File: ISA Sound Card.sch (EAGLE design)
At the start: 60 parts, among them IC1 74LS07D, IC2 74AHC1G07DBV, U1 PCM1808, U10 SN74LVC16T245DGGR, U11 SN74LVC16T245DGGR, U12 SN74LVC16T245DGGR, U3 MIC5365-3.3YD5-TR, U4 PCM5102, U5 SN74LVC16T245DGGR, U7 MIC5365-3.3YD5-TR, U8 SN74LVC16T245DGGR, U9 SN74LVC16T245DGGR, X2 LINE_OUT, X3 LINE_IN

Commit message: First routing done, DRC passed. MIDI and Waveblaster are todo
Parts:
- removed F1, F2: 500mA, adafruit:PTCFUSE-1206
- added C10, C11, C12, C13, C14, C3, C4, C5, C6, C7, C8, C9: 100nF, rcl:C-EUC0603
- added F3, F5, F6: 500mA, adafruit:PTCFUSE-1206
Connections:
- removed net -5V: ISAB.-5VDC
- new net MIDI_RXD: U$512.F
- new net MIDI_TXD: U$515.F
- new net N$13: F3.2, ISAB.+5VDC@1
- new net N$14: F5.2, ISAB.-12VDC
- new net N$27: F6.2, ISAB.+12VDC
- net +12V: now also F5.1; no longer ISAB.-12VDC
- net +3V3: now also C10.1, C11.1, C12.1, C13.1, C14.1, C9.1, U$1G$1.+3V3@3, U$1G$1.+3V3@4, U$1G$2.+3V3@3, U$1G$2.+3V3@4
- net +5V: now also C3.1, C4.1, C5.1, C6.1, C7.1, C8.1, F3.1, JP1.10, JP1.14, JP1.6, U$51.F, U$58.F, U$59.F; no longer F1.2, F2.2, ISAB.+5VDC@1
- net -12V: now also F6.1; no longer ISAB.+12VDC
- net GND: now also C10.2, C11.2, C12.2, C13.2, C14.2, C3.2, C4.2, C5.2, C6.2, C7.2, C8.2, C9.2; no longer U$512.F
- net N$5: now also U$1G$3.FPGA_DCLK; no longer F1.1, JP1.10, JP1.14, JP1.6
- net N$6: now also U$1G$3.FPGA_ADS0; no longer F2.1, U$51.F, U$515.F, U$58.F, U$59.F
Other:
- note added: "TODO - MIDI voltage translation and FPGA hookup"
- moved on the sheet: ISAA, ISAB, ISAC, ISAD, R1, R2, R3, U10, U11, U12, U5, U8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

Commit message: Had to change IRQ/DRQ buffers for muxes. Not routed yet
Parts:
- removed F5, F6: 500mA, adafruit:PTCFUSE-1206
- removed JP1: (no value), pinhead:PINHD-2X13
- removed U5, U9: SN74LVC16T245DGGR, SN74LVC16T245DGGR:SN74LVC16T245DGGR
- added C15, C16, C17, C18: 100nF, rcl:C-EUC0805
- added C19, C20, C21, C22: 100nF, rcl:C-EUC0603
- added IC10, IC11, IC8, IC9: 4051D, 40xx:4051D
- added IC3: 74AC14D, 74xx-eu:74AC14D
- added IC4: 74LVC1G125DBV, 74xx-little-de:74LVC1G125DBV
- added R10, R7, R8, R9: 4K7, rcl:R-EU_R0603
- added RN2: 10K, resistor-dil:4R-N0603-ARC
- added RN3: 2K2, resistor-dil:4R-N0603-ARC
- added U$2: MCP3004, adafruit:MCP3004
- RN1: value (none) -> 2K2
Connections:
- net N$5 renamed FPGA_DCLK
- net N$6 renamed FPGA_ADS0
- removed net +12V: F5.1, JP1.18
- removed net -12V: F6.1, JP1.22
- removed net FPGA_DRQ0: U$1G$2.BANK4A_U17, U5.1B8
- removed net FPGA_DRQ1: U$1G$1.BANK7A_H11, U9.2B1
- removed net FPGA_DRQ2: U$1G$2.BANK3B_U12, U9.1B6
- removed net FPGA_DRQ3: U$1G$2.BANK3B_V9, U9.1B8
- removed net FPGA_DRQ5: U$1G$1.BANK7A_C18, U5.2B1
- removed net FPGA_DRQ6: U$1G$2.BANK4A_AB17, U5.2B2
- removed net FPGA_DRQ7: U$1G$1.BANK7A_C19, U5.2B3
- removed net FPGA_IRQ10: U$1G$1.BANK7A_B18, U5.1B3
- removed net FPGA_IRQ11: U$1G$2.BANK5A_R16, U5.1B4
- removed net FPGA_IRQ12: U$1G$1.BANK7A_A17, U5.1B5
- removed net FPGA_IRQ14: U$1G$1.BANK7A_A18, U5.1B7
- removed net FPGA_IRQ15: U$1G$2.BANK4A_U16, U5.1B6
- removed net FPGA_IRQ3: U$1G$2.BANK3B_AB11, U9.2B6
- removed net FPGA_IRQ4: U$1G$1.BANK7A_D12, U9.2B5
- removed net FPGA_IRQ5: U$1G$2.BANK3B_AB10, U9.2B4
- removed net FPGA_IRQ6: U$1G$1.BANK7A_E12, U9.2B3
- removed net FPGA_IRQ7: U$1G$2.BANK3B_V10, U9.2B2
- removed net FPGA_IRQ9: U$1G$1.BANK8A_A10, U9.1B5
- removed net GAME_B1_N: U$52.F
- removed net GAME_B2_N: U$57.F
- removed net GAME_B3_N: U$510.F
- removed net GAME_B4_N: U$514.F
- removed net GAME_X1: U$53.F
- removed net GAME_X2: U$511.F
- removed net GAME_Y: U$513.F
- removed net GAME_Y1: U$56.F
- removed net N$10: U$1G$1.BANK8A_B6
- removed net N$12: U$1G$1.BANK8A_J7
- removed net N$16: U$1G$2.BANK3A_N6
- removed net N$17: U$1G$2.BANK3A_R5
- removed net N$18: U$1G$2.BANK3A_M6
- removed net N$19: U$1G$2.BANK3A_P6
- removed net N$20: U$1G$2.BANK3A_R6
- removed net N$26: U$1G$2.BANK3B_AA8
- removed net N$3: U$1G$1.BANK8A_A5
- removed net N$4: U$1G$1.BANK8A_C6
- removed net N$7: U$1G$2.BANK4A_AB18
- removed net WAVL: JP1.20
- removed net WAVR: JP1.24
- removed net WAV_MIDI: JP1.4
- removed net WAV_RST_N: JP1.26
- new net DRQ_HI_SEL_A0: IC11A.A, U$1G$1.BANK7A_C18
- new net DRQ_HI_SEL_A1: IC11A.B, U$1G$1.BANK7A_A18
- new net DRQ_HI_SEL_A2: IC11A.C, U$1G$1.BANK7A_A17
- new net DRQ_HI_TRIG_N: IC11A.INH, R10.1, U$1G$1.BANK7A_C19
- new net DRQ_LO_SEL_A0: IC10A.A, U$1G$2.BANK4A_AB17
- new net DRQ_LO_SEL_A1: IC10A.B, U$1G$2.BANK4A_U17
- new net DRQ_LO_SEL_A2: IC10A.C, U$1G$2.BANK4A_U16
- new net DRQ_LO_TRIG_N: IC10A.INH, R9.1, U$1G$2.BANK4A_AB18
- new net FPGA_JOY_B1: IC3A.O, U$1G$2.BANK3A_M6
- new net FPGA_JOY_B2: IC3B.O, U$1G$2.BANK3A_N6
- new net FPGA_JOY_B3: IC3C.O, U$1G$2.BANK3A_P6
- new net FPGA_JOY_B4: IC3D.O, U$1G$2.BANK3A_R5
- new net FPGA_MIDI_RXD: IC3E.O, U$1G$2.BANK3A_R6
- new net FPGA_MIDI_TXD: IC4A.I, U$1G$2.BANK3B_AA8
- new net IRQ_HI_SEL_A0: IC9A.A, U$1G$1.BANK7A_E12
- new net IRQ_HI_SEL_A1: IC9A.B, U$1G$1.BANK7A_H11
- new net IRQ_HI_SEL_A2: IC9A.C, U$1G$1.BANK8A_A10
- new net IRQ_HI_TRIG_N: IC9A.INH, R8.1, U$1G$1.BANK7A_D12
- new net IRQ_LO_SEL_A0: IC8A.A, U$1G$2.BANK3B_AB11
- new net IRQ_LO_SEL_A1: IC8A.B, U$1G$2.BANK3B_V9
- new net IRQ_LO_SEL_A2: IC8A.C, U$1G$2.BANK3B_V10
- new net IRQ_LO_TRIG_N: IC8A.INH, R7.1, U$1G$2.BANK3B_AB10
- new net JOY_B1_N: IC3A.I, U$52.F
- new net JOY_B2_N: IC3B.I, U$57.F
- new net JOY_B3_N: IC3C.I, U$510.F
- new net JOY_B4_N: IC3D.I, U$514.F
- new net JOY_CLK: U$1G$1.BANK8A_C6, U$2.CLK
- new net JOY_CS_N: U$1G$1.BANK8A_J7, U$2./CS
- new net JOY_DIN: U$1G$1.BANK8A_A8, U$2.DIN
- new net JOY_DOUT: U$1G$1.BANK8A_B6, U$2.DOUT
- new net JOY_X1: RN2A.1, U$53.F
- new net JOY_X2: RN2B.1, U$511.F
- new net JOY_Y1: RN2D.1, U$56.F
- new net JOY_Y2: RN2C.1, U$513.F
- new net N$15: RN2D.2, RN3A.2, U$2.CH3
- new net N$28: RN2C.2, RN3B.2, U$2.CH2
- new net N$31: RN2B.2, RN3C.2, U$2.CH1
- new net N$32: RN2A.2, RN3D.2, U$2.CH0
- new net N$34: IC3F.O
- new net N$41: IC3F.I
- net +3V3: now also C15.1, C16.1, C17.1, IC3P.VCC, R10.2, R7.2, R8.2, R9.2, U$2.VDD, U$2.VREF; no longer U5.VCCB_18, U5.VCCB_7, U9.VCCB_18, U9.VCCB_7
- net +5V: now also C18.1, C19.1, C20.1, C21.1, C22.1, IC10A.X, IC10P.VCC, IC11A.X, IC11P.VCC, IC4P.VCC, IC8A.X, IC8P.VCC, IC9A.X, IC9P.VCC; no longer JP1.10, JP1.14, JP1.6, U5.VCCA_31, U5.VCCA_42, U9.VCCA_31, U9.VCCA_42
- net DRQ0: now also IC10A.X0, IC11A.X0; no longer U5.1A8
- net DRQ1: now also IC10A.X1, IC11A.X1; no longer U9.2A1
- net DRQ2: now also IC10A.X2, IC11A.X2; no longer U9.1A6
- net DRQ3: now also IC10A.X3, IC11A.X3; no longer U9.1A8
- net DRQ5: now also IC10A.X5, IC11A.X5; no longer U5.2A1
- net DRQ6: now also IC10A.X6, IC11A.X6; no longer U5.2A2
- net DRQ7: now also IC10A.X7, IC11A.X7; no longer U5.2A3
- net FPGA_SD70_DIR: now also U$1G$1.BANK8A_A5; no longer U$1G$1.BANK8A_A8
- net GND: now also C15.2, C16.2, C17.2, C18.2, C19.2, C20.2, C21.2, C22.2, IC10P.GND, IC10P.VEE, IC11P.GND, IC11P.VEE, IC3P.GND, IC4A.OE, IC4P.GND, IC8P.GND, IC8P.VEE, IC9P.GND, IC9P.VEE, RN3A.1, RN3B.1, RN3C.1, RN3D.1, U$2.AGND, U$2.DGND; no longer JP1.1, JP1.11, JP1.15, JP1.17, JP1.19, JP1.21, JP1.23, JP1.25, JP1.3, JP1.5, JP1.7, JP1.9, U5.1!OE, U5.1DIR, U5.2!OE, U5.2DIR, U5.GND_10, U5.GND_15, U5.GND_21, U5.GND_28, U5.GND_34, U5.GND_39, U5.GND_4, U5.GND_45, U9.1!OE, U9.1DIR, U9.2!OE, U9.2DIR, U9.GND_10, U9.GND_15, U9.GND_21, U9.GND_28, U9.GND_34, U9.GND_39, U9.GND_4, U9.GND_45
- net IRQ10: now also IC8A.X3, IC9A.X3; no longer U5.1A3
- net IRQ11: now also IC8A.X4, IC9A.X4; no longer U5.1A4
- net IRQ12: now also IC8A.X5, IC9A.X5; no longer U5.1A5
- net IRQ14: now also IC8A.X6, IC9A.X6; no longer U5.1A7
- net IRQ15: now also IC8A.X7, IC9A.X7; no longer U5.1A6
- net IRQ3: no longer U9.2A6
- net IRQ4: no longer U9.2A5
- net IRQ5: now also IC8A.X0, IC9A.X0; no longer U9.2A4
- net IRQ6: now also IC8A.X1, IC9A.X1; no longer U9.2A3
- net IRQ7: now also IC8A.X2, IC9A.X2; no longer U9.2A2
- net IRQ9: no longer U9.1A5
- net MIDI_RXD: now also IC3E.I
- net MIDI_TXD: now also IC4A.O
- net N$14: no longer F5.2
- net N$27: no longer F6.2
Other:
- note removed: "<- OUTPUTS"
- note removed: "TODO - MIDI voltage translation and FPGA hookup"
- note removed: "WaveBlaster Header"

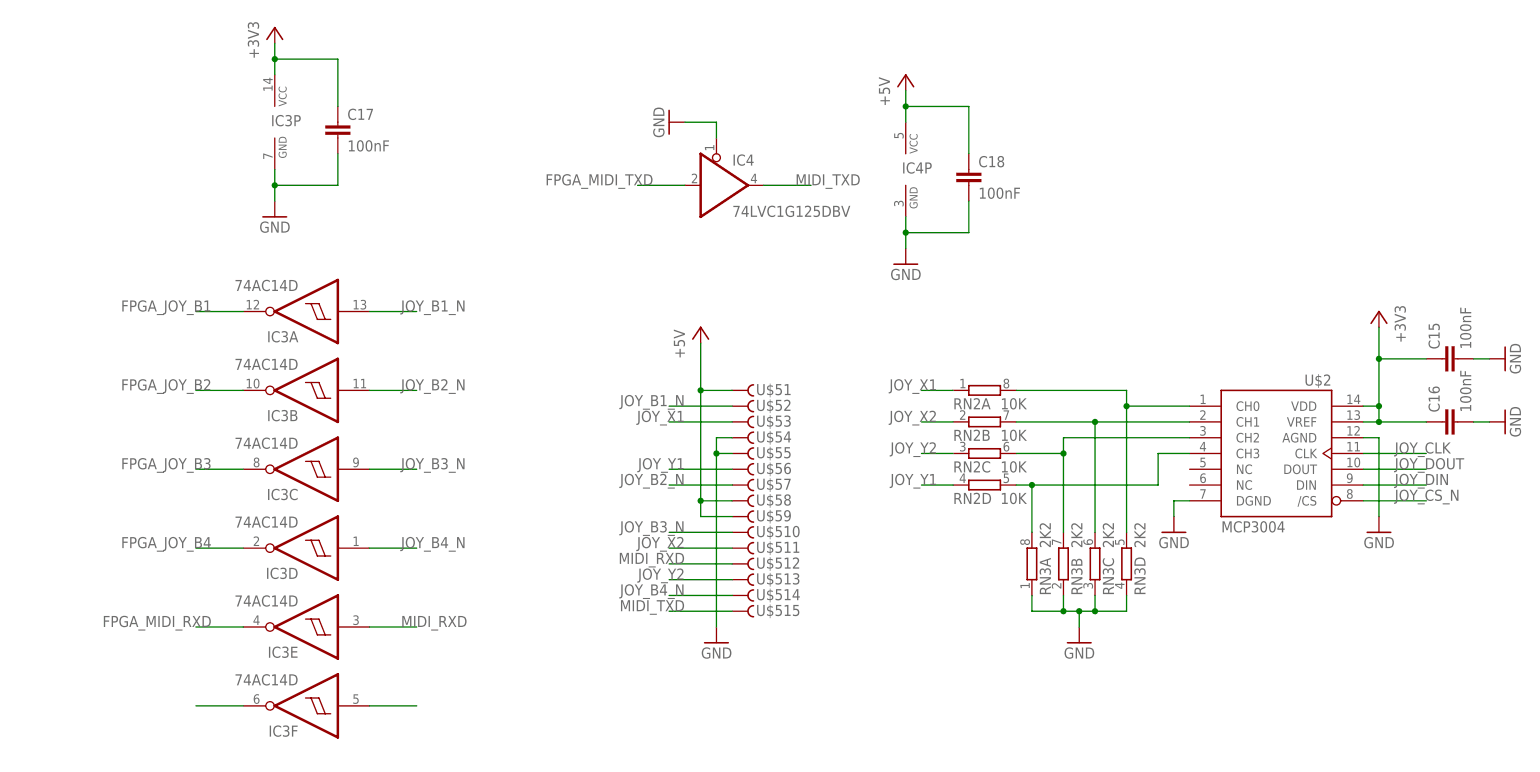
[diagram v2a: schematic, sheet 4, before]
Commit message: Routing done. Fixed two missing signals. Five proto PCBs being made by JLC
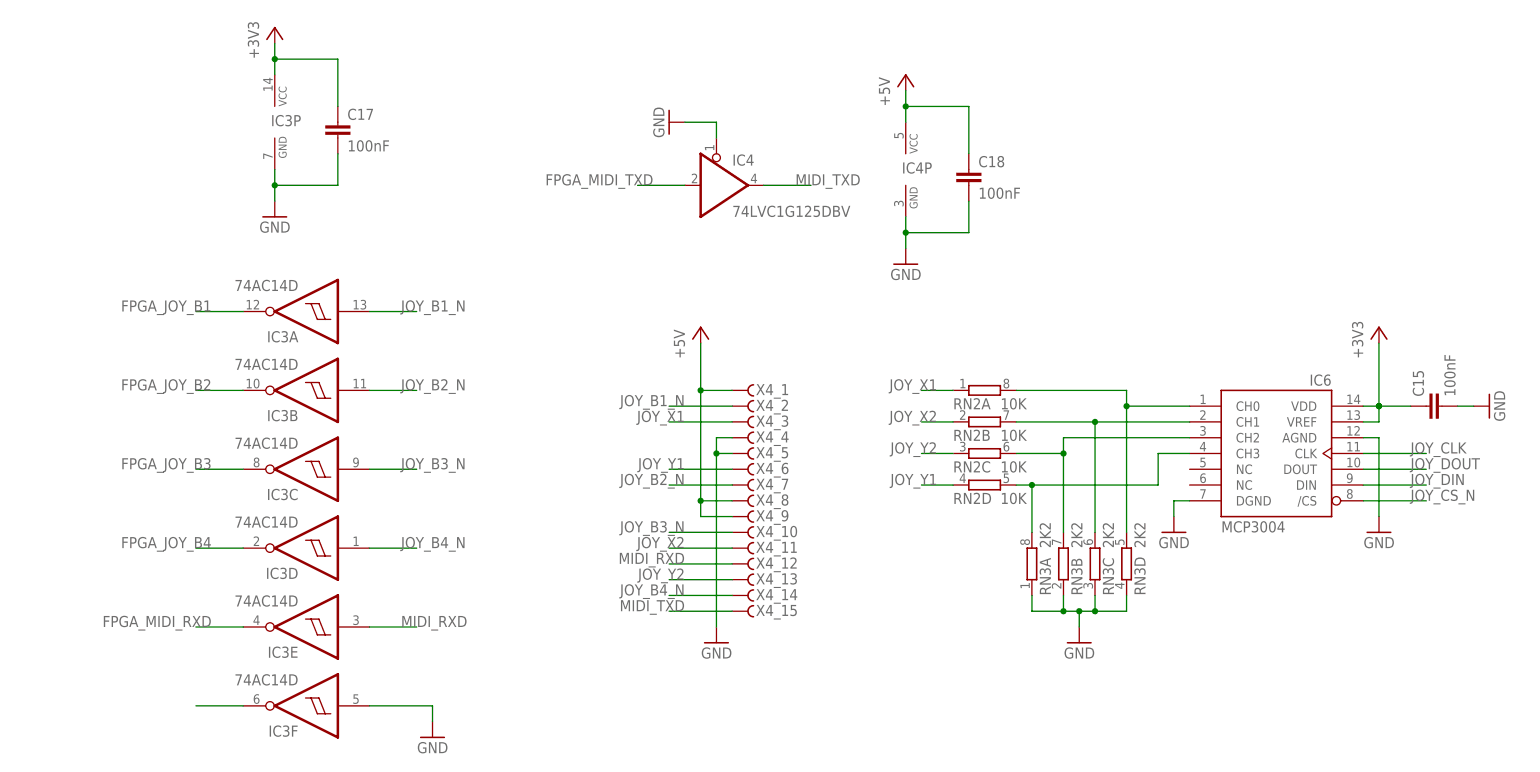
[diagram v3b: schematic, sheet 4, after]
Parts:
- removed C16: 100nF, rcl:C-EUC0805
- added R11: 4K7, rcl:R-EU_R0603
- renumbered U$2 to IC6, U$5 to X4_
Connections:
- removed net +5VDC: ISAD.+5VDC
- removed net FPGA_MEMW_R: U11.1B2
- removed net N$11: U$1G$1.BANK7A_A14
- removed net N$41: IC3F.I
- new net FPGA_MEMW_N: U$1G$1.BANK7A_A15, U11.1B2
- new net FPGA_SA159_DIR: R11.2, U$1G$2.BANK3B_U12, U8.1DIR, U8.2DIR
- net +3V3: now also R11.1; no longer C16.1, U8.1DIR, U8.2DIR
- net +5V: now also ISAD.+5VDC
- net FPGA_BALE: now also U$1G$1.BANK7A_C16; no longer U$1G$1.BANK7A_C15
- net FPGA_DACK0_N: now also U$1G$1.BANK7A_B16; no longer U$1G$1.BANK7A_C16
- net FPGA_DACK2_N: now also U$1G$1.BANK7A_C15; no longer U$1G$1.BANK7A_B15
- net FPGA_DACK3_N: now also U$1G$1.BANK7A_E15; no longer U$1G$1.BANK7A_F15
- net FPGA_DACK6_N: now also U$1G$1.BANK7A_B18; no longer U$1G$1.BANK7A_B16
- net FPGA_IOW_N: now also U$1G$1.BANK7A_F15; no longer U$1G$1.BANK7A_A15
- net FPGA_MEMR_N: now also U$1G$1.BANK7A_A14
- net FPGA_SD159_DIR: now also U$1G$1.BANK7A_B15; no longer U$1G$1.BANK7A_E15
- net GND: now also IC3F.I; no longer C16.2
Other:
- note added: "INPUTS -> (Added DIR control anyway)"
- moved on the sheet: C15

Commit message: Updated Eagle symbols for the QMTech CycIV version
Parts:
- removed U$1: QMTECH_5CEFA5F23_SMD, qmtech:QMTECH_5CEFA5F23_SMD
- added CYC_IV_: QMTECH_EP4CE15, qmtech:QMTECH_EP4CE15
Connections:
- net +3V3: now also CYC_IV_G$1.+3V3@3, CYC_IV_G$1.+3V3@4, CYC_IV_G$2.+3V3@3, CYC_IV_G$2.+3V3@4; no longer U$1G$1.+3V3@3, U$1G$1.+3V3@4, U$1G$2.+3V3@3, U$1G$2.+3V3@4
- net +5V: now also CYC_IV_G$1.VIN@63, CYC_IV_G$1.VIN@64, CYC_IV_G$2.VIN@63, CYC_IV_G$2.VIN@64; no longer U$1G$1.VIN@63, U$1G$1.VIN@64, U$1G$2.VIN@63, U$1G$2.VIN@64
- net ADC_DOUT: now also CYC_IV_G$2.B19@57; no longer U$1G$2.BANK3B_AB7
- net CONF_DONE: now also CYC_IV_G$3.CONF_DONE; no longer U$1G$3.CONF_DONE
- net DAC_DIN: now also CYC_IV_G$2.A20@60; no longer U$1G$2.BANK3B_AB6
- net DRQ_HI_SEL_A0: now also CYC_IV_G$1.AB17@16; no longer U$1G$1.BANK7A_C18
- net DRQ_HI_SEL_A1: now also CYC_IV_G$1.AA18@17; no longer U$1G$1.BANK7A_A18
- net DRQ_HI_SEL_A2: now also CYC_IV_G$1.AB18@18; no longer U$1G$1.BANK7A_A17
- net DRQ_HI_TRIG_N: now also CYC_IV_G$1.AA17@15; no longer U$1G$1.BANK7A_C19
- net DRQ_LO_SEL_A0: now also CYC_IV_G$2.J2@16; no longer U$1G$2.BANK4A_AB17
- net DRQ_LO_SEL_A1: now also CYC_IV_G$2.H1@17; no longer U$1G$2.BANK4A_U17
- net DRQ_LO_SEL_A2: now also CYC_IV_G$2.H2@18; no longer U$1G$2.BANK4A_U16
- net DRQ_LO_TRIG_N: now also CYC_IV_G$2.J1@15; no longer U$1G$2.BANK4A_AB18
- net FPGA_0WS: now also CYC_IV_G$1.L21@40; no longer U$1G$1.BANK7A_G12
- net FPGA_ADS0: now also CYC_IV_G$3.FPGA_ADS0; no longer U$1G$3.FPGA_ADS0
- net FPGA_AEN: now also CYC_IV_G$1.H22@45; no longer U$1G$1.BANK8A_E9
- net FPGA_BALE: now also CYC_IV_G$1.AB20@22; no longer U$1G$1.BANK7A_C16
- net FPGA_CLK: now also CYC_IV_G$2.B1@25; no longer U$1G$2.BANK4A_AA15
- net FPGA_DACK0_N: now also CYC_IV_G$1.AA20@21; no longer U$1G$1.BANK7A_B16
- net FPGA_DACK1_N: now also CYC_IV_G$2.B2@26; no longer U$1G$2.BANK4A_AB15
- net FPGA_DACK2_N: now also CYC_IV_G$1.Y22@23; no longer U$1G$1.BANK7A_C15
- net FPGA_DACK3_N: now also CYC_IV_G$1.W22@25; no longer U$1G$1.BANK7A_E15
- net FPGA_DACK5_N: now also CYC_IV_G$2.D2@22; no longer U$1G$2.BANK5A_R15
- net FPGA_DACK6_N: now also CYC_IV_G$1.AA19@19; no longer U$1G$1.BANK7A_B18
- net FPGA_DACK7_N: now also CYC_IV_G$2.E1@21; no longer U$1G$2.BANK5A_T15
- net FPGA_DCLK: now also CYC_IV_G$3.FPGA_DCLK; no longer U$1G$3.FPGA_DCLK
- net FPGA_IOCHK: now also CYC_IV_G$1.E21@50; no longer U$1G$1.BANK8A_K7
- net FPGA_IOCHRDY: now also CYC_IV_G$1.M19@60; no longer U$1G$1.BANK8A_B5
- net FPGA_IOCS16_N: now also CYC_IV_G$1.B21@56; no longer U$1G$1.BANK8A_B7
- net FPGA_IOR_N: now also CYC_IV_G$2.B3@27; no longer U$1G$2.BANK4A_T13
- net FPGA_IOW_N: now also CYC_IV_G$1.W21@26; no longer U$1G$1.BANK7A_F15
- net FPGA_JOY_B1: now also CYC_IV_G$2.A15@50; no longer U$1G$2.BANK3A_M6
- net FPGA_JOY_B2: now also CYC_IV_G$2.B16@51; no longer U$1G$2.BANK3A_N6
- net FPGA_JOY_B3: now also CYC_IV_G$2.A16@52; no longer U$1G$2.BANK3A_P6
- net FPGA_JOY_B4: now also CYC_IV_G$2.B17@53; no longer U$1G$2.BANK3A_R5
- net FPGA_LA17: now also CYC_IV_G$2.N1@11; no longer U$1G$2.BANK4A_AA20
- net FPGA_LA18: now also CYC_IV_G$1.AA15@11; no longer U$1G$1.BANK7A_C20
- net FPGA_LA19: now also CYC_IV_G$2.N2@12; no longer U$1G$2.BANK4A_AA19
- net FPGA_LA20: now also CYC_IV_G$1.AB15@12; no longer U$1G$1.BANK7A_B20
- net FPGA_LA21: now also CYC_IV_G$2.M1@13; no longer U$1G$2.BANK4A_W19
- net FPGA_LA22: now also CYC_IV_G$1.AA16@13; no longer U$1G$1.BANK7A_A20
- net FPGA_LA23: now also CYC_IV_G$2.M2@14; no longer U$1G$2.BANK4A_V20
- net FPGA_LA_DIR: now also CYC_IV_G$1.AB19@20; no longer U$1G$1.BANK7A_B17
- net FPGA_MASTER_N: now also CYC_IV_G$1.N19@58; no longer U$1G$1.BANK8A_D6
- net FPGA_MEMCS16_N: now also CYC_IV_G$1.C21@54; no longer U$1G$1.BANK8A_A7
- net FPGA_MEMR_N: now also CYC_IV_G$1.V21@28; no longer U$1G$1.BANK7A_A14
- net FPGA_MEMW_N: now also CYC_IV_G$1.V22@27; no longer U$1G$1.BANK7A_A15
- net FPGA_MIDI_RXD: now also CYC_IV_G$2.A17@54; no longer U$1G$2.BANK3A_R6
- net FPGA_MIDI_TXD: now also CYC_IV_G$2.A18@56; no longer U$1G$2.BANK3B_AA8
- net FPGA_OSC: now also CYC_IV_G$2.C1@23; no longer U$1G$2.BANK4A_R14
- net FPGA_REFRESH_N: now also CYC_IV_G$1.D21@52; no longer U$1G$1.BANK8A_J8
- net FPGA_RES_DRV: now also CYC_IV_G$2.B10@43; no longer U$1G$2.BANK3B_R9
- net FPGA_SA0: now also CYC_IV_G$2.B4@29; no longer U$1G$2.BANK3B_R11
- net FPGA_SA1: now also CYC_IV_G$1.U22@29; no longer U$1G$1.BANK7A_B13
- net FPGA_SA10: now also CYC_IV_G$2.A5@34; no longer U$1G$2.BANK4A_Y14
- net FPGA_SA11: now also CYC_IV_G$1.P21@34; no longer U$1G$1.BANK7A_F14
- net FPGA_SA12: now also CYC_IV_G$2.B6@35; no longer U$1G$2.BANK4A_AB12
- net FPGA_SA13: now also CYC_IV_G$1.N22@35; no longer U$1G$1.BANK7A_H13
- net FPGA_SA14: now also CYC_IV_G$2.A6@36; no longer U$1G$2.BANK4A_AB13
- net FPGA_SA15: now also CYC_IV_G$1.N21@36; no longer U$1G$1.BANK7A_G13
- net FPGA_SA159_DIR: now also CYC_IV_G$2.B9@41; no longer U$1G$2.BANK3B_U12
- net FPGA_SA16: now also CYC_IV_G$1.J22@43; no longer U$1G$1.BANK8A_J9
- net FPGA_SA17: now also CYC_IV_G$2.A10@44; no longer U$1G$2.BANK3B_T10
- net FPGA_SA18: now also CYC_IV_G$1.J21@44; no longer U$1G$1.BANK8A_H9
- net FPGA_SA19: now also CYC_IV_G$2.B13@45; no longer U$1G$2.BANK3A_T8
- net FPGA_SA2: now also CYC_IV_G$2.A4@30; no longer U$1G$2.BANK3B_R10
- net FPGA_SA3: now also CYC_IV_G$1.U21@30; no longer U$1G$1.BANK7A_A13
- net FPGA_SA4: now also CYC_IV_G$2.C4@31; no longer U$1G$2.BANK4A_AA13
- net FPGA_SA5: now also CYC_IV_G$1.R22@31; no longer U$1G$1.BANK7A_B12
- net FPGA_SA6: now also CYC_IV_G$2.C3@32; no longer U$1G$2.BANK4A_AA14
- net FPGA_SA7: now also CYC_IV_G$1.R21@32; no longer U$1G$1.BANK7A_A12
- net FPGA_SA8: now also CYC_IV_G$2.B5@33; no longer U$1G$2.BANK4A_Y15
- net FPGA_SA9: now also CYC_IV_G$1.P22@33; no longer U$1G$1.BANK7A_G15
- net FPGA_SBHE: now also CYC_IV_G$1.AB16@14; no longer U$1G$1.BANK7A_A19
- net FPGA_SD0: now also CYC_IV_G$2.A13@46; no longer U$1G$2.BANK3A_T7
- net FPGA_SD1: now also CYC_IV_G$1.H21@46; no longer U$1G$1.BANK8A_D9
- net FPGA_SD10: now also CYC_IV_G$1.AA14@9; no longer U$1G$1.BANK7A_E19
- net FPGA_SD11: now also CYC_IV_G$2.P1@9; no longer U$1G$2.BANK4A_Y19
- net FPGA_SD12: now also CYC_IV_G$1.AB13@8; no longer U$1G$1.BANK7A_F18
- net FPGA_SD13: now also CYC_IV_G$2.R2@8; no longer U$1G$2.BANK4A_AB20
- net FPGA_SD14: now also CYC_IV_G$1.AA13@7; no longer U$1G$1.BANK7A_F19
- net FPGA_SD15: now also CYC_IV_G$2.R1@7; no longer U$1G$2.BANK4A_AB21
- net FPGA_SD159_DIR: now also CYC_IV_G$1.Y21@24; no longer U$1G$1.BANK7A_B15
- net FPGA_SD2: now also CYC_IV_G$2.B14@47; no longer U$1G$2.BANK3B_N8
- net FPGA_SD3: now also CYC_IV_G$1.F22@47; no longer U$1G$1.BANK8A_H8
- net FPGA_SD4: now also CYC_IV_G$2.A14@48; no longer U$1G$2.BANK3B_P8
- net FPGA_SD5: now also CYC_IV_G$1.F21@48; no longer U$1G$1.BANK8A_G8
- net FPGA_SD6: now also CYC_IV_G$2.B15@49; no longer U$1G$2.BANK3A_M7
- net FPGA_SD7: now also CYC_IV_G$1.E22@49; no longer U$1G$1.BANK8A_L7
- net FPGA_SD70_DIR: now also CYC_IV_G$1.M20@59; no longer U$1G$1.BANK8A_A5
- net FPGA_SD8: now also CYC_IV_G$1.AB14@10; no longer U$1G$1.BANK7A_D19
- net FPGA_SD9: now also CYC_IV_G$2.P2@10; no longer U$1G$2.BANK4A_Y20
- net FPGA_SMEMR_N: now also CYC_IV_G$2.A9@42; no longer U$1G$2.BANK3B_U11
- net FPGA_SMEMW_N: now also CYC_IV_G$1.K21@42; no longer U$1G$1.BANK8A_A9
- net FPGA_TC: now also CYC_IV_G$2.C2@24; no longer U$1G$2.BANK4A_P14
- net GND: now also CYC_IV_G$1.CLK14_6N@6, CYC_IV_G$1.CLK15_6P@5, CYC_IV_G$1.GND@1, CYC_IV_G$1.GND@2, CYC_IV_G$1.GND@61, CYC_IV_G$1.GND@62, CYC_IV_G$2.GND@1, CYC_IV_G$2.GND@2, CYC_IV_G$2.GND@5, CYC_IV_G$2.GND@6, CYC_IV_G$2.GND@61, CYC_IV_G$2.GND@62, CYC_IV_G$3.GND; no longer U$1G$1.GND@1, U$1G$1.GND@2, U$1G$1.GND@5, U$1G$1.GND@6, U$1G$1.GND@61, U$1G$1.GND@62, U$1G$2.GND@1, U$1G$2.GND@2, U$1G$2.GND@5, U$1G$2.GND@6, U$1G$2.GND@61, U$1G$2.GND@62, U$1G$3.GND
- net I2S_BCK: now also CYC_IV_G$2.A19@58; no longer U$1G$2.BANK3B_AA7
- net I2S_LRCK: now also CYC_IV_G$2.B20@59; no longer U$1G$2.BANK3B_AB5
- net I2S_SCK: now also CYC_IV_G$2.B18@55; no longer U$1G$2.BANK3B_AB8
- net IRQ_HI_SEL_A0: now also CYC_IV_G$1.M21@38; no longer U$1G$1.BANK7A_E12
- net IRQ_HI_SEL_A1: now also CYC_IV_G$1.L22@39; no longer U$1G$1.BANK7A_H11
- net IRQ_HI_SEL_A2: now also CYC_IV_G$1.K22@41; no longer U$1G$1.BANK8A_A10
- net IRQ_HI_TRIG_N: now also CYC_IV_G$1.M22@37; no longer U$1G$1.BANK7A_D12
- net IRQ_LO_SEL_A0: now also CYC_IV_G$2.B7@37; no longer U$1G$2.BANK3B_AB11
- net IRQ_LO_SEL_A1: now also CYC_IV_G$2.A8@40; no longer U$1G$2.BANK3B_V9
- net IRQ_LO_SEL_A2: now also CYC_IV_G$2.B8@39; no longer U$1G$2.BANK3B_V10
- net IRQ_LO_TRIG_N: now also CYC_IV_G$2.A7@38; no longer U$1G$2.BANK3B_AB10
- net JOY_CLK: now also CYC_IV_G$1.N20@57; no longer U$1G$1.BANK8A_C6
- net JOY_CS_N: now also CYC_IV_G$1.D22@51; no longer U$1G$1.BANK8A_J7
- net JOY_DIN: now also CYC_IV_G$1.C22@53; no longer U$1G$1.BANK8A_A8
- net JOY_DOUT: now also CYC_IV_G$1.B22@55; no longer U$1G$1.BANK8A_B6
- net N$8: now also CYC_IV_G$2.F2@20; no longer U$1G$2.BANK5A_R17
- net N$9: now also CYC_IV_G$2.A3@28; no longer U$1G$2.BANK4A_T12
- net NCONFIG: now also CYC_IV_G$3.NCONFIG; no longer U$1G$3.NCONFIG
- net NSTATUS: now also CYC_IV_G$3.NSTATUS; no longer U$1G$3.NSTATUS
